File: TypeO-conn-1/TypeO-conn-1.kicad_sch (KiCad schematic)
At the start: 5 parts

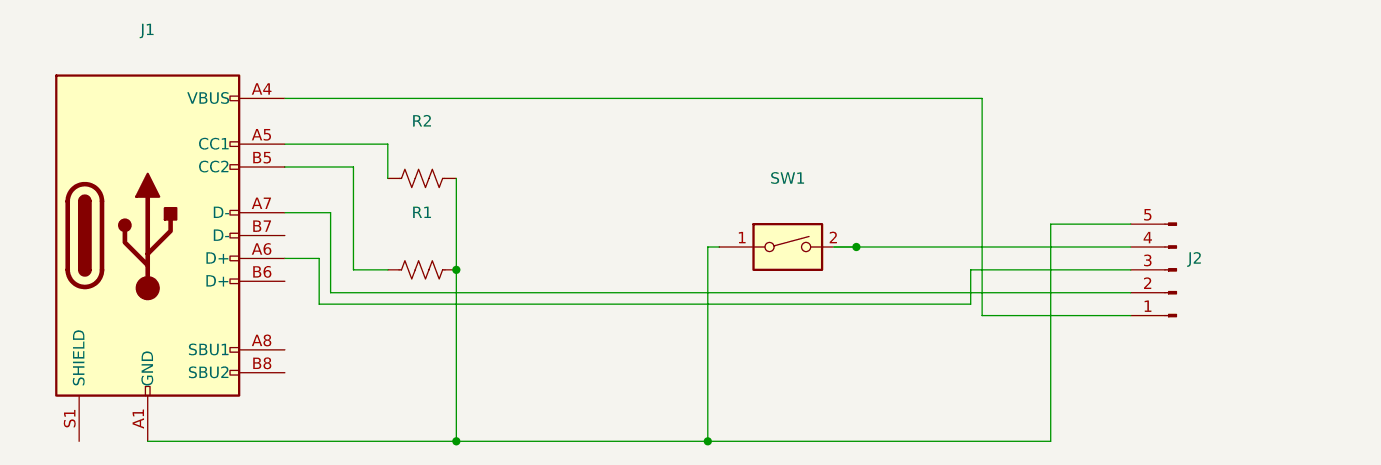
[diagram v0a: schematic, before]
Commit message: Update PCB to add jumpers
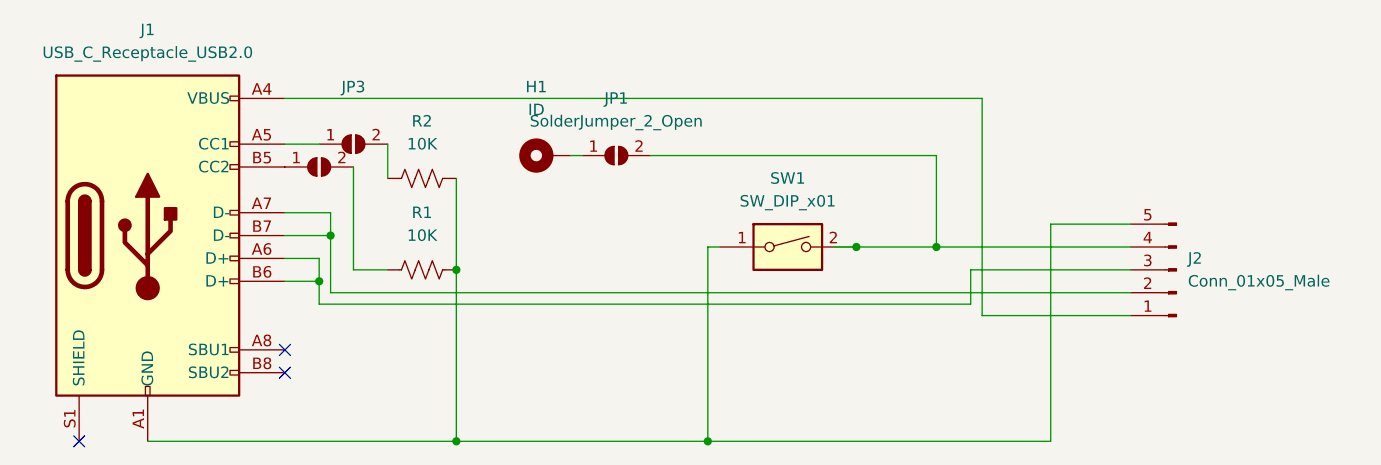
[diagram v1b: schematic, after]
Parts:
- added H1: ID, Connector_Wire:SolderWire-0.1sqmm_1x01_D0.4mm_OD1mm, symbol Mechanical:MountingHole_Pad
- added JP1: SolderJumper_2_Open, Jumper:SolderJumper-2_P1.3mm_Open_TrianglePad1.0x1.5mm, symbol Jumper:SolderJumper_2_Open
- added JP2, JP3: (no value), symbol Jumper:SolderJumper_2_Open
- J1: value (none) -> USB_C_Receptacle_USB2.0; footprint (none) -> Connector_USB:USB_C_Receptacle_JAE_DX07S016JA1R1500
- J2: value (none) -> Conn_01x05_Male; footprint (none) -> Connector_PinHeader_2.54mm:PinHeader_1x05_P2.54mm_Vertical
- R1, R2: value (none) -> 10K; footprint (none) -> Resistor_THT:R_Axial_DIN0207_L6.3mm_D2.5mm_P7.62mm_Horizontal
- SW1: value (none) -> SW_DIP_x01; footprint (none) -> Button_Switch_SMD:SW_DIP_SPSTx01_Slide_Omron_A6S-110x_W8.9mm_P2.54mm
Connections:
- net at J1.A5 (CC1): now also JP3.1 (A); no longer R2.2
- net at J1.A6 (D+), J2.3 (Pin_3): now also J1.B6 (D+)
- net at J1.A7 (D-), J2.2 (Pin_2): now also J1.B7 (D-)
- net at J1.B5 (CC2): now also JP2.1 (A); no longer R1.2
- net at J2.4 (Pin_4), SW1.2: now also JP1.2 (B)
- new net: JP2.2 (B), R1.2
- new net: JP3.2 (B), R2.2
- new net: H1.1, JP1.1 (A)
- no-connect marks 0 -> 3
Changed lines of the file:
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@@
 (kicad_sch (version 20211123) (generator eeschema)
   (paper "A4")
+  (junction (at 57.15 93.98) (diameter 0) (color 0 0 0 0)
+  )
   (junction (at 72.39 92.71) (diameter 0) (color 0 0 0 0)
   )
+  (junction (at 58.42 88.9) (diameter 0) (color 0 0 0 0)
+  )
   (junction (at 116.84 90.17) (diameter 0) (color 0 0 0 0)
   )
@@
   (junction (at 72.39 111.76) (diameter 0) (color 0 0 0 0)
   )
-  (wire (pts (xy 116.84 90.17) (xy 147.32 90.17))
+  (junction (at 125.73 90.17) (diameter 0) (color 0 0 0 0)
+  )
+  (no_connect (at 53.34 101.6))
+  (no_connect (at 53.34 104.14))
+  (no_connect (at 30.48 111.76))
+  (wire (pts (xy 116.84 90.17) (xy 125.73 90.17))
     (stroke (width 0) (type default) (color 0 0 0 0))
   )
@@
     (stroke (width 0) (type default) (color 0 0 0 0))
   )
-  (wire (pts (xy 60.96 81.28) (xy 53.34 81.28))
+  (wire (pts (xy 58.42 88.9) (xy 58.42 95.25))
     (stroke (width 0) (type default) (color 0 0 0 0))
   )
@@
     (stroke (width 0) (type default) (color 0 0 0 0))
   )
-  (wire (pts (xy 58.42 86.36) (xy 58.42 95.25))
+  (wire (pts (xy 58.42 86.36) (xy 58.42 88.9))
+    (stroke (width 0) (type default) (color 0 0 0 0))
+  )
+  (wire (pts (xy 64.77 78.74) (xy 64.77 82.55))
     (stroke (width 0) (type default) (color 0 0 0 0))
   )
@@
     (stroke (width 0) (type default) (color 0 0 0 0))
   )
-  (wire (pts (xy 64.77 78.74) (xy 64.77 82.55))
-    (stroke (width 0) (type default) (color 0 0 0 0))
-  )
   (wire (pts (xy 138.43 111.76) (xy 138.43 87.63))
     (stroke (width 0) (type default) (color 0 0 0 0))
@@
     (stroke (width 0) (type default) (color 0 0 0 0))
   )
-  (wire (pts (xy 53.34 78.74) (xy 64.77 78.74))
+  (wire (pts (xy 125.73 90.17) (xy 147.32 90.17))
+    (stroke (width 0) (type default) (color 0 0 0 0))
+  )
+  (wire (pts (xy 53.34 78.74) (xy 57.15 78.74))
+    (stroke (width 0) (type default) (color 0 0 0 0))
+  )
+  (wire (pts (xy 125.73 80.01) (xy 125.73 90.17))
+    (stroke (width 0) (type default) (color 0 0 0 0))
+  )
+  (wire (pts (xy 93.98 80.01) (xy 125.73 80.01))
     (stroke (width 0) (type default) (color 0 0 0 0))
   )
@@
     (stroke (width 0) (type default) (color 0 0 0 0))
   )
+  (wire (pts (xy 86.36 80.01) (xy 85.09 80.01))
+    (stroke (width 0) (type default) (color 0 0 0 0))
+  )
+  (wire (pts (xy 53.34 88.9) (xy 58.42 88.9))
+    (stroke (width 0) (type default) (color 0 0 0 0))
+  )
+  (wire (pts (xy 53.34 93.98) (xy 57.15 93.98))
+    (stroke (width 0) (type default) (color 0 0 0 0))
+  )
+  (wire (pts (xy 57.15 93.98) (xy 57.15 96.52))
+    (stroke (width 0) (type default) (color 0 0 0 0))
+  )
   (wire (pts (xy 60.96 92.71) (xy 60.96 81.28))
     (stroke (width 0) (type default) (color 0 0 0 0))
@@
     (stroke (width 0) (type default) (color 0 0 0 0))
   )
-  (wire (pts (xy 57.15 91.44) (xy 57.15 96.52))
+  (wire (pts (xy 57.15 91.44) (xy 57.15 93.98))
     (stroke (width 0) (type default) (color 0 0 0 0))
   )
@@
     (in_bom yes) (on_board yes) (fields_autoplaced)
     (property "Reference" "J1" (id 0) (at 38.1 66.04 0))
-    (property "Value" "" (id 1) (at 38.1 68.58 0))
-    (property "Footprint" "" (id 2) (at 41.91 88.9 0)
+    (property "Value" "USB_C_Receptacle_USB2.0" (id 1) (at 38.1 68.58 0))
+    (property "Footprint" "Connector_USB:USB_C_Receptacle_JAE_DX07S016JA1R1500" (id 2) (at 41.91 88.9 0)
       (effects (font (size 1.27 1.27)) hide)
     )
@@
       (effects (font (size 1.27 1.27)) (justify right))
     )
-    (property "Value" "" (id 1) (at 153.67 93.9799 0)
+    (property "Value" "Conn_01x05_Male" (id 1) (at 153.67 93.9799 0)
       (effects (font (size 1.27 1.27)) (justify right))
     )
-    (property "Footprint" "" (id 2) (at 152.4 92.71 0)
+    (property "Footprint" "Connector_PinHeader_2.54mm:PinHeader_1x05_P2.54mm_Vertical" (id 2) (at 152.4 92.71 0)
       (effects (font (size 1.27 1.27)) hide)
     )
@@
     (in_bom yes) (on_board yes) (fields_autoplaced)
     (property "Reference" "SW1" (id 0) (at 109.22 82.55 0))
-    (property "Value" "" (id 1) (at 109.22 85.09 0))
-    (property "Footprint" "" (id 2) (at 109.22 90.17 0)
+    (property "Value" "SW_DIP_x01" (id 1) (at 109.22 85.09 0))
+    (property "Footprint" "Button_Switch_SMD:SW_DIP_SPSTx01_Slide_Omron_A6S-110x_W8.9mm_P2.54mm" (id 2) (at 109.22 90.17 0)
       (effects (font (size 1.27 1.27)) hide)
     )
@@
     (pin "2")
   )
+  (symbol (lib_id "Jumper:SolderJumper_2_Open") (at 57.15 81.28 0) (unit 1)
+    (in_bom yes) (on_board yes)
+    (property "Reference" "JP2" (id 0) (at 57.15 83.82 0)
+      (effects (font (size 1.27 1.27)) hide)
+    )
+    (property "Value" "" (id 1) (at 57.15 83.82 0))
+    (property "Footprint" "" (id 2) (at 57.15 81.28 0)
+      (effects (font (size 1.27 1.27)) hide)
+    )
+    (property "Datasheet" "~" (id 3) (at 57.15 81.28 0)
+      (effects (font (size 1.27 1.27)) hide)
+    )
+    (pin "1")
+    (pin "2")
+  )
   (symbol (lib_id "Device:R_US") (at 68.58 92.71 270) (unit 1)
     (in_bom yes) (on_board yes) (fields_autoplaced)
     (property "Reference" "R1" (id 0) (at 68.58 86.36 90))
-    (property "Value" "" (id 1) (at 68.58 88.9 90))
-    (property "Footprint" "" (id 2) (at 68.326 93.726 90)
+    (property "Value" "10K" (id 1) (at 68.58 88.9 90))
+    (property "Footprint" "Resistor_THT:R_Axial_DIN0207_L6.3mm_D2.5mm_P7.62mm_Horizontal" (id 2) (at 68.326 93.726 90)
       (effects (font (size 1.27 1.27)) hide)
     )
@@
     (pin "2")
   )
+  (symbol (lib_id "Jumper:SolderJumper_2_Open") (at 60.96 78.74 0) (unit 1)
+    (in_bom yes) (on_board yes)
+    (property "Reference" "JP3" (id 0) (at 60.96 72.39 0))
+    (property "Value" "" (id 1) (at 60.96 76.2 0))
+    (property "Footprint" "" (id 2) (at 60.96 78.74 0)
+      (effects (font (size 1.27 1.27)) hide)
+    )
+    (property "Datasheet" "~" (id 3) (at 60.96 78.74 0)
+      (effects (font (size 1.27 1.27)) hide)
+    )
+    (pin "1")
+    (pin "2")
+  )
+  (symbol (lib_id "Jumper:SolderJumper_2_Open") (at 90.17 80.01 0) (unit 1)
+    (in_bom yes) (on_board yes) (fields_autoplaced)
+    (property "Reference" "JP1" (id 0) (at 90.17 73.66 0))
+    (property "Value" "SolderJumper_2_Open" (id 1) (at 90.17 76.2 0))
+    (property "Footprint" "Jumper:SolderJumper-2_P1.3mm_Open_TrianglePad1.0x1.5mm" (id 2) (at 90.17 80.01 0)
+      (effects (font (size 1.27 1.27)) hide)
+    )
+    (property "Datasheet" "~" (id 3) (at 90.17 80.01 0)
+      (effects (font (size 1.27 1.27)) hide)
+    )
+    (pin "1")
+    (pin "2")
+  )
+  (symbol (lib_id "Mechanical:MountingHole_Pad") (at 82.55 80.01 90) (unit 1)
+    (in_bom yes) (on_board yes) (fields_autoplaced)
+    (property "Reference" "H1" (id 0) (at 81.28 72.39 90))
+    (property "Value" "ID" (id 1) (at 81.28 74.93 90))
+    (property "Footprint" "Connector_Wire:SolderWire-0.1sqmm_1x01_D0.4mm_OD1mm" (id 2) (at 82.55 80.01 0)
+      (effects (font (size 1.27 1.27)) hide)
+    )
+    (property "Datasheet" "~" (id 3) (at 82.55 80.01 0)
+      (effects (font (size 1.27 1.27)) hide)
+    )
+    (pin "1")
+  )
   (symbol (lib_id "Device:R_US") (at 68.58 82.55 270) (unit 1)
     (in_bom yes) (on_board yes) (fields_autoplaced)
     (property "Reference" "R2" (id 0) (at 68.58 76.2 90))
-    (property "Value" "" (id 1) (at 68.58 78.74 90))
-    (property "Footprint" "" (id 2) (at 68.326 83.566 90)
+    (property "Value" "10K" (id 1) (at 68.58 78.74 90))
+    (property "Footprint" "Resistor_THT:R_Axial_DIN0207_L6.3mm_D2.5mm_P7.62mm_Horizontal" (id 2) (at 68.326 83.566 90)
       (effects (font (size 1.27 1.27)) hide)
     )
@@
   )
   (symbol_instances
+    (path "/d75139c9-6bbf-4bff-a021-8da65b8dbc4a"
+      (reference "H1") (unit 1) (value "ID") (footprint "Connector_Wire:SolderWire-0.1sqmm_1x01_D0.4mm_OD1mm")
+    )
     (path "/1199146e-a60b-416a-b503-e77d6d2892f9"
       (reference "J1") (unit 1) (value "USB_C_Receptacle_USB2.0") (footprint "Connector_USB:USB_C_Receptacle_JAE_DX07S016JA1R1500")
@@
       (reference "J2") (unit 1) (value "Conn_01x05_Male") (footprint "Connector_PinHeader_2.54mm:PinHeader_1x05_P2.54mm_Vertical")
     )
+    (path "/aa594b1f-fd74-46a0-a124-e1d2aed26358"
+      (reference "JP1") (unit 1) (value "SolderJumper_2_Open") (footprint "Jumper:SolderJumper-2_P1.3mm_Open_TrianglePad1.0x1.5mm")
+    )
+    (path "/407fae1f-316c-420a-89e6-21f138123cbe"
+      (reference "JP2") (unit 1) (value "CC2") (footprint "Jumper:SolderJumper-2_P1.3mm_Open_RoundedPad1.0x1.5mm")
+    )
+    (path "/a66a3b2f-f268-4e38-987e-b27ec003ce16"
+      (reference "JP3") (unit 1) (value "CC1") (footprint "Jumper:SolderJumper-2_P1.3mm_Open_RoundedPad1.0x1.5mm")
+    )
     (path "/7342cc82-e0e9-41f9-8b46-68197771b07f"
